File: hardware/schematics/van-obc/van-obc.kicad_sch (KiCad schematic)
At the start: 0 parts

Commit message: Add KiCad schematics for Van Onboard Computer (v1.0)
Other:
- added sheet Display_And_UI (Display_And_UI.kicad_sch)
- added sheet MCU_Arduino_Mega (MCU_Arduino_Mega.kicad_sch)
- added sheet Power_Input (Power_Input.kicad_sch)
- added sheet Power_Monitoring (Power_Monitoring.kicad_sch)
- added sheet Sensors (Sensors.kicad_sch)
- title: (none) -> Van Onboard Computer

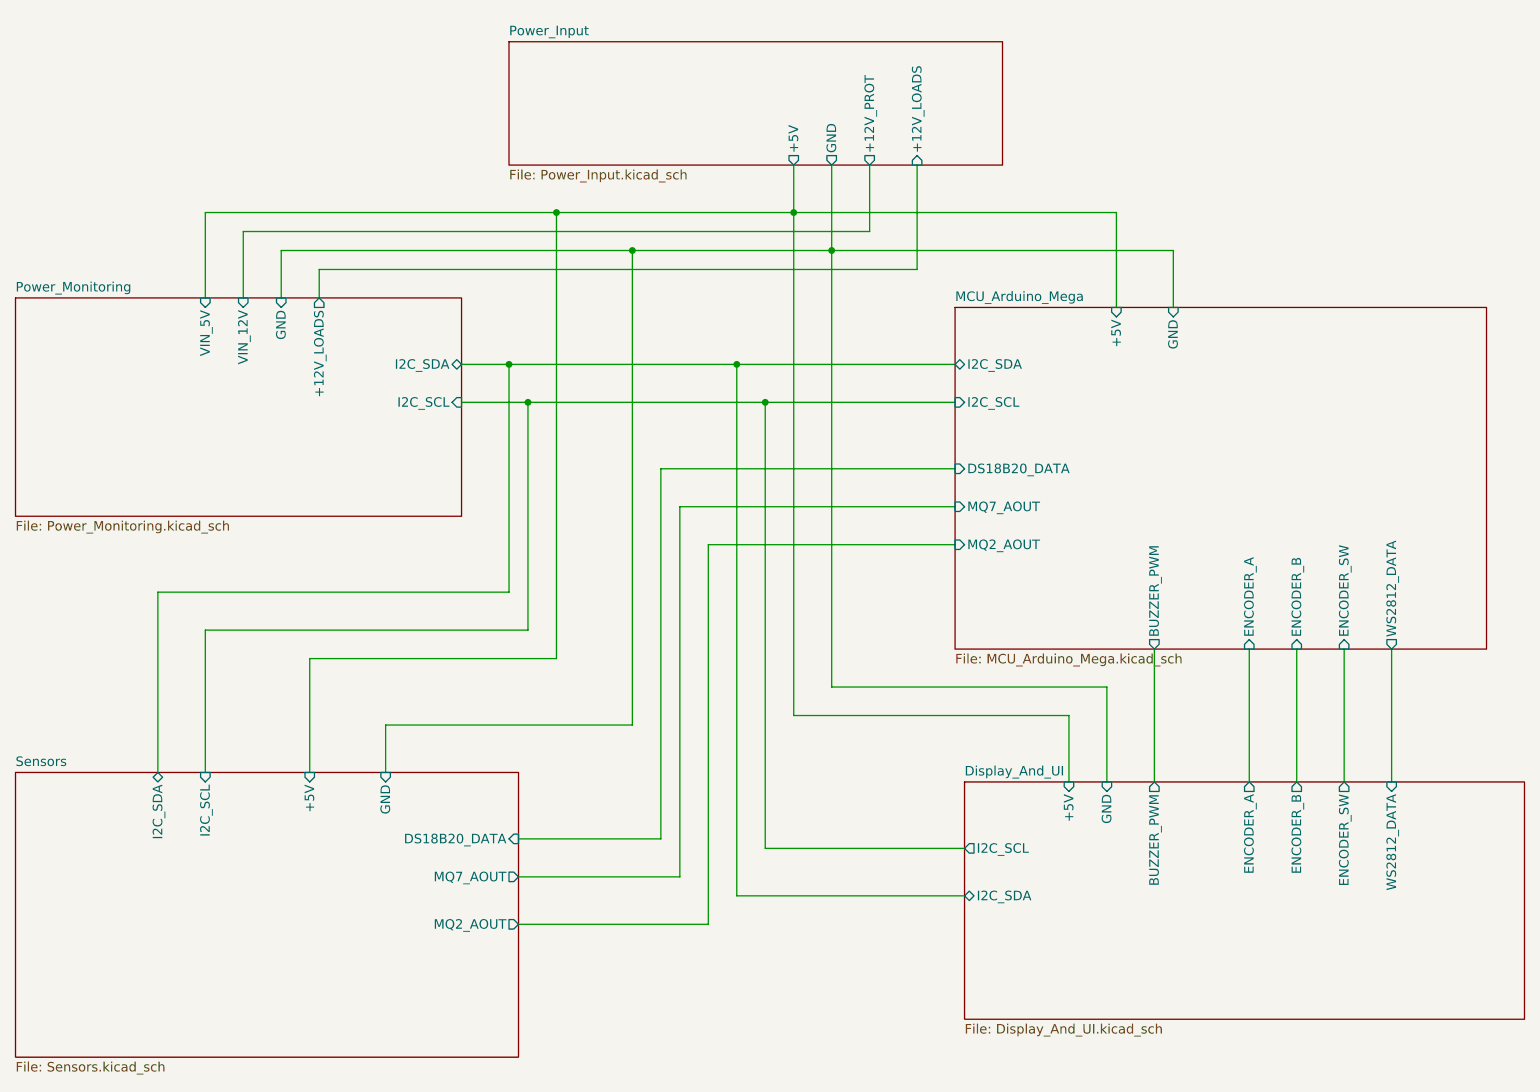
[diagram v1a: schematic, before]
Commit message: fix(tests): Corrections majeures KY040, BME280, MPU6050
- KY040 v2.1.0: Fix comptage + anti-rebond capacitif
- BME280 v1.0.1: Fix begin() avec &Wire
- MPU6050 v2.0.0: Simplification (acc only, dérive <2°)
- Ajout diagnostic_bme280.ino + CHANGELOG

Tests: 6/11 validés (55%)
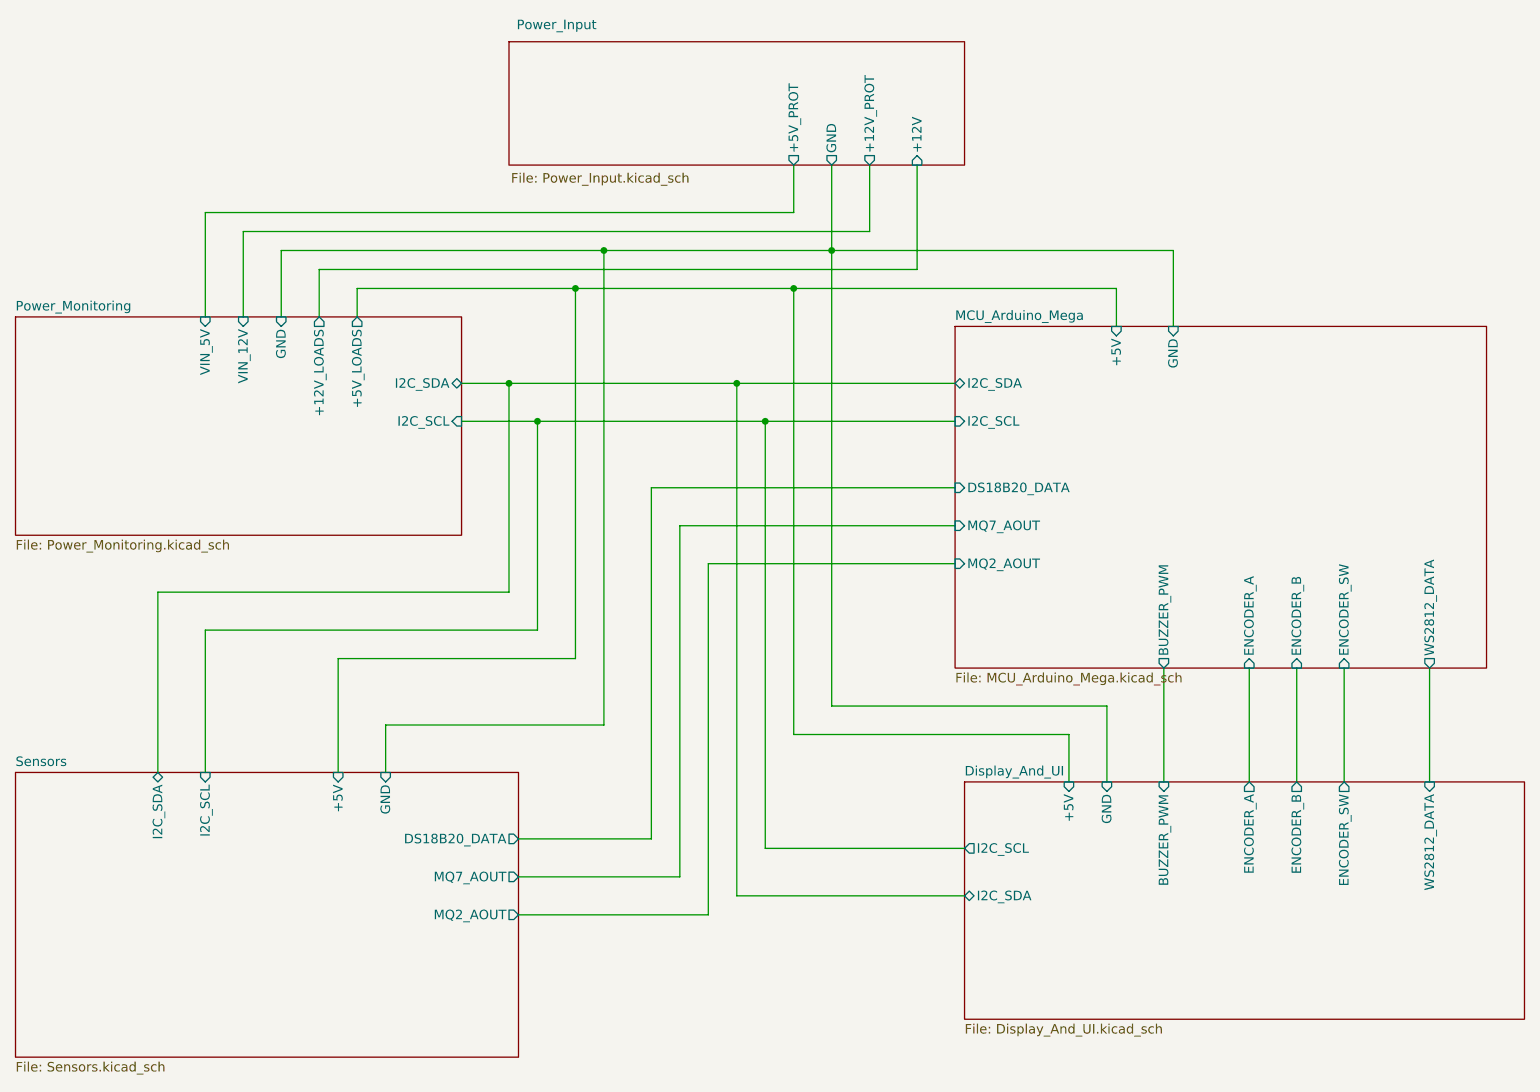
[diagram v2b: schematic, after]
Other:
- sheet Power_Input ports: added +12V, +5V_PROT; removed +12V_LOADS, +5V
- sheet Power_Monitoring ports: added +5V_LOADS; removed none
